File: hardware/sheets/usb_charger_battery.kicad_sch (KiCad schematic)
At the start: 0 parts

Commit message: hw: draw Rev A power tree and USB charger sheets
Power tree: TPS63802 3.3 V logic rail, TPS61023 LED rail with load
disconnect, switched VBAT measurement, VLED sense, 0-ohm measurement
links and test points. The logic rail is enabled by the power switch
or by the charger's power-good output, so USB starts a charging-only
state with the switch off and removing USB turns the rail off again.
The LED rail and VBAT measurement default off.

Charger: USB-C sink with separate 5.1 kOhm Rd, TPD4E05U06 on D+, D-,
CC1 and CC2, isolated CC sensing, BQ25620 switching charger with BC1.2
detection, a board NTC on TS, and the JST-PH battery header.

The VLED setting is provisional until LED testing. The battery header
polarity is provisional until checked against the pack, and the USB-C
receptacle part is still to be chosen.
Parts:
- added C301, C302: 100nF, Capacitor_SMD:C_0402_1005Metric, symbol Device:C
- added C303: 1uF 50V, Capacitor_SMD:C_0603_1608Metric, symbol Device:C
- added C304, C309: 10uF 25V, Capacitor_SMD:C_0805_2012Metric, symbol Device:C
- added C305: 47nF 16V, Capacitor_SMD:C_0402_1005Metric, symbol Device:C
- added C306: 4.7uF 16V, Capacitor_SMD:C_0603_1608Metric, symbol Device:C
- added C307, C308: 22uF 25V, Capacitor_SMD:C_0805_2012Metric, symbol Device:C
- added J301: USB-C receptacle (part TBD), symbol Connector:USB_C_Receptacle_USB2.0_16P
- added J302: Battery JST-PH 2P, Connector_JST:JST_PH_B2B-PH-SM4-TB_1x02-1MP_P2.00mm_Vertical, symbol Connector_Generic_MountingPin:Conn_01x02_MountingPin
- added L301: 1uH, smart-led-badge:L_Coilcraft_XEL4030, symbol Device:L
- added Q301, Q302: AO3400A, Package_TO_SOT_SMD:SOT-23, symbol Transistor_FET:AO3400A
- added R301, R302: 5.1k, Resistor_SMD:R_0402_1005Metric, symbol Device:R
- added R303, R306, R313: 100k, Resistor_SMD:R_0402_1005Metric, symbol Device:R
- added R304, R307: 12k, Resistor_SMD:R_0402_1005Metric, symbol Device:R
- added R309: 5.23k, Resistor_SMD:R_0402_1005Metric, symbol Device:R
- added R310: 30.1k, Resistor_SMD:R_0402_1005Metric, symbol Device:R
- added R311, R312: 10k, Resistor_SMD:R_0402_1005Metric, symbol Device:R
- added R314, R315: 4.7k, Resistor_SMD:R_0402_1005Metric, symbol Device:R
- added TH301: 10k B3380/3434, Resistor_SMD:R_0402_1005Metric, symbol Device:Thermistor_NTC
- added TP301: VBUS, TestPoint:TestPoint_Pad_D1.0mm, symbol Connector:TestPoint
- added TP302: PMID, TestPoint:TestPoint_Pad_D1.0mm, symbol Connector:TestPoint
- added TP303: SYS, TestPoint:TestPoint_Pad_D1.0mm, symbol Connector:TestPoint
- added TP304: VBAT, TestPoint:TestPoint_Pad_D1.0mm, symbol Connector:TestPoint
- added TP305: TS, TestPoint:TestPoint_Pad_D1.0mm, symbol Connector:TestPoint
- added TP306: CHG_PG_N, TestPoint:TestPoint_Pad_D1.0mm, symbol Connector:TestPoint
- added TP307: QON, TestPoint:TestPoint_Pad_D1.0mm, symbol Connector:TestPoint
- added TP308: CHG_STAT, TestPoint:TestPoint_Pad_D1.0mm, symbol Connector:TestPoint
- added TP309: CC1, TestPoint:TestPoint_Pad_D1.0mm, symbol Connector:TestPoint
- added TP310: CC2, TestPoint:TestPoint_Pad_D1.0mm, symbol Connector:TestPoint
- added TP311: GND, TestPoint:TestPoint_Pad_D1.0mm, symbol Connector:TestPoint
- added TP312: I2C1_SDA, TestPoint:TestPoint_Pad_D1.0mm, symbol Connector:TestPoint
- added TP313: I2C1_SCL, TestPoint:TestPoint_Pad_D1.0mm, symbol Connector:TestPoint
- added U301: TPD4E05U06, Package_SON:USON-10_2.5x1.0mm_P0.5mm, symbol Power_Protection:TPD4E05U06DQA
- added U302: BQ25620, smart-led-badge:Texas_RYK0018A, symbol smart-led-badge:BQ25620
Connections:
- new net +3V3: Q301.1 (G), Q302.1 (G), R311.2, R312.2, R314.2, R315.2
- new net BTST: C305.1, U302.1 (BTST)
- new net CC1: J301.A5 (CC1), R301.1, R303.1, TP309.1, U301.4 (D2+)
- new net CC1_HV: Q301.3 (D), R303.2
- new net CC1_SENSE: C301.1, Q301.2 (S), R304.1
- new net CC2: J301.B5 (CC2), R302.1, R306.1, TP310.1, U301.5 (D2-)
- new net CC2_HV: Q302.3 (D), R306.2
- new net CC2_SENSE: C302.1, Q302.2 (S), R307.1
- new net CHG_CE: R313.1, U302.14 (CE)
- new net CHG_INT: R312.1, U302.11 (INT)
- new net CHG_PG_N: TP306.1, U302.3 (PG)
- new net CHG_STAT: R311.1, TP308.1, U302.10 (STAT)
- new net GND: C301.2, C302.2, C303.2, C304.2, C306.2, C307.2, C308.2, C309.2, J301.A1 (GND), J301.A12 (GND), J301.B1 (GND), J301.B12 (GND), J301.SH (SHIELD), J302.1 (Pin_1), J302.MP (MountPin), R301.2, R302.2, R304.2, R307.2, R310.2, R313.2, TH301.2, TP311.1, U301.3 (GND), U301.8 (GND), U302.15 (GND)
- new net I2C1_SCL: R315.1, TP313.1, U302.13 (SCL)
- new net I2C1_SDA: R314.1, TP312.1, U302.12 (SDA)
- new net PMID: C304.1, TP302.1, U302.17 (PMID)
- new net QON: TP307.1, U302.7 (QON)
- new net REGN: C306.1, R309.1, U302.2 (REGN)
- new net SW_CHG: C305.2, L301.1, U302.16 (SW)
- new net SYS: C307.1, C308.1, L301.2, TP303.1, U302.9 (SYS)
- new net TS: R309.2, R310.1, TH301.1, TP305.1, U302.6 (TS)
- new net USB_DN: J301.A7 (D-), J301.B7 (D-), U301.2 (D1-), U302.4 (D-)
- new net USB_DP: J301.A6 (D+), J301.B6 (D+), U301.1 (D1+), U302.5 (D+)
- new net VBAT: C309.1, J302.2 (Pin_2), TP304.1, U302.8 (BAT)
- new net VBUS: C303.1, J301.A4 (VBUS), J301.A9 (VBUS), J301.B4 (VBUS), J301.B9 (VBUS), TP301.1, U302.18 (VBUS)
- no-connect marks 0 -> 6
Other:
- note added: "USB-C, charger and battery (Rev A) - design notes USB-C sink, USB 2.0, no PD: independent 5.1k Rd on CC1/CC2; TPD4E05U06 on D+, D-, CC1, CC2. CC sense: firmware reads CC1/CC2 via SAADC (ratio 0.107) and raises the BQ25620 input limit only on a valid >= 1.5 A advertisement; SDP/unknown sources stay at 100 mA until USB enumeration. BQ25620 (SLUSEG2D): switching charger with NVDC power path, BC1.2 o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"

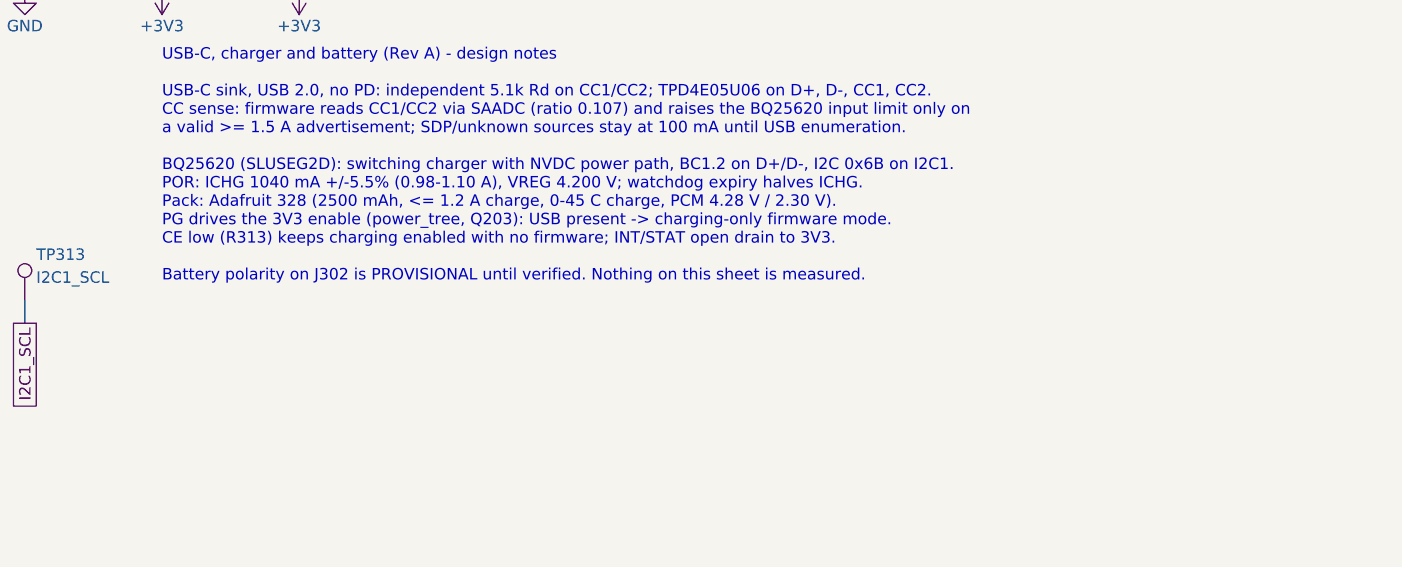
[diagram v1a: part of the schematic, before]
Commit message: hw: set battery header polarity from Adafruit pinout
Keep pin 1 = BAT- and pin 2 = BAT+ on the JST PH header, and record
why: Adafruit's own USB-C Micro-Lipo charger wires its JST PH battery
connector the same way, and Adafruit states the 2500 mAh pack matches
its boards. The "reverse plug" note on the cell drawing describes
that wiring, not a further swap.

No pack is available yet, so bring-up meter-checks each pack before
its first connection.
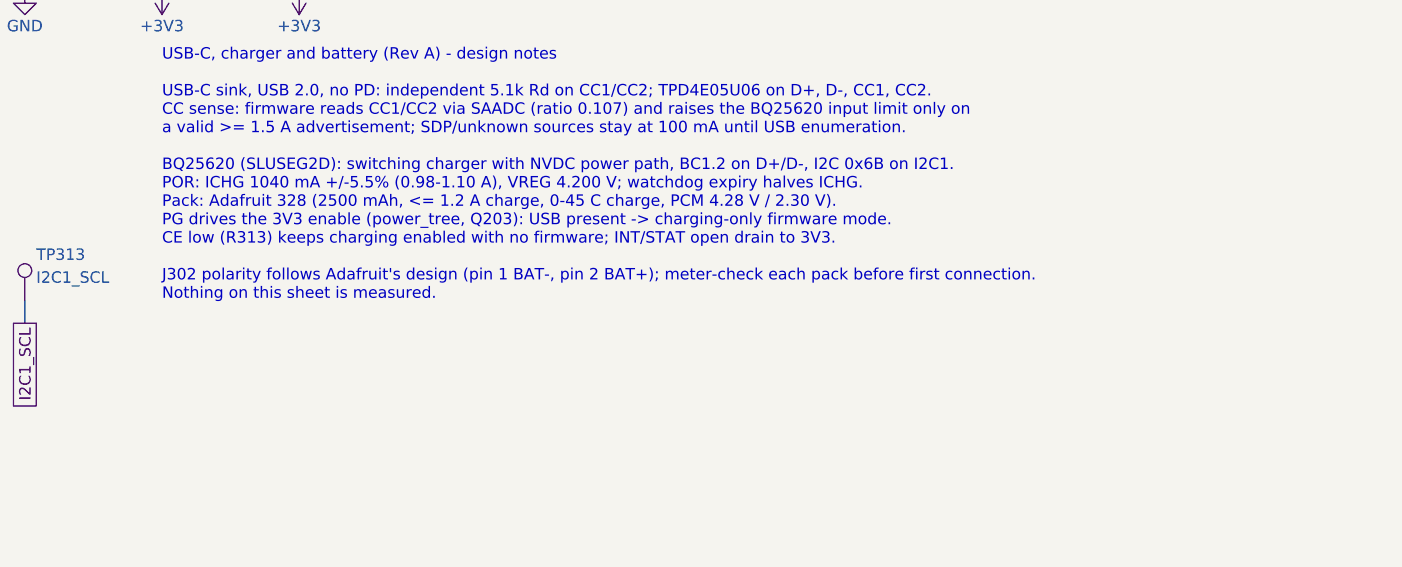
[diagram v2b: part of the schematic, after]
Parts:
- J302: Note POLARITY PROVISIONAL: pin 1 = BAT-, pin 2 = BAT+ until veri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 -> Pin 1 = BAT-, pin 2 = BAT+ per Adafruit's own charger desig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
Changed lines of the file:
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@@
 			)
 		)
-		(property "Note" "POLARITY PROVISIONAL: pin 1 = BAT-, pin 2 = BAT+ until verified against the JST drawing and the Adafruit 328 pack (open decision)"
+		(property "Note" "Pin 1 = BAT-, pin 2 = BAT+ per Adafruit's own charger design (Micro-Lipo USB-C CN2: pin 1 GND, pin 2 VBAT) and Adafruit's statement that product 328 matches its boards; meter-check the pack before first connection"
 			(at 33.02 165.1 0)
 			(hide yes)
@@
 		)
 	)
-	(text "USB-C, charger and battery (Rev A) - design notes\n\nUSB-C sink, USB 2.0, no PD: independent 5.1k Rd on CC1/CC2; TPD4E05U06 on D+, D-, CC1, CC2.\nCC sense: firmware reads CC1/CC2 via SAADC (ratio 0.107) and raises the BQ25620 input limit only on\na valid >= 1.5 A advertisement; SDP/unknown sources stay at 100 mA until USB enumeration.\n\nBQ25620 (SLUSEG2D): switching charger with NVDC power path, BC1.2 on D+/D-, I2C 0x6B on I2C1.\nPOR: ICHG 1040 mA +/-5.5% (0.98-1.10 A), VREG 4.200 V; watchdog expiry halves ICHG.\nPack: Adafruit 328 (2500 mAh, <= 1.2 A charge, 0-45 C charge, PCM 4.28 V / 2.30 V).\nPG drives the 3V3 enable (power_tree, Q203): USB present -> charging-only firmware mode.\nCE low (R313) keeps charging enabled with no firmware; INT/STAT open drain to 3V3.\n\nBattery polarity on J302 is PROVISIONAL until verified. Nothing on this sheet is measured."
+	(text "USB-C, charger and battery (Rev A) - design notes\n\nUSB-C sink, USB 2.0, no PD: independent 5.1k Rd on CC1/CC2; TPD4E05U06 on D+, D-, CC1, CC2.\nCC sense: firmware reads CC1/CC2 via SAADC (ratio 0.107) and raises the BQ25620 input limit only on\na valid >= 1.5 A advertisement; SDP/unknown sources stay at 100 mA until USB enumeration.\n\nBQ25620 (SLUSEG2D): switching charger with NVDC power path, BC1.2 on D+/D-, I2C 0x6B on I2C1.\nPOR: ICHG 1040 mA +/-5.5% (0.98-1.10 A), VREG 4.200 V; watchdog expiry halves ICHG.\nPack: Adafruit 328 (2500 mAh, <= 1.2 A charge, 0-45 C charge, PCM 4.28 V / 2.30 V).\nPG drives the 3V3 enable (power_tree, Q203): USB present -> charging-only firmware mode.\nCE low (R313) keeps charging enabled with no firmware; INT/STAT open drain to 3V3.\n\nJ302 polarity follows Adafruit's design (pin 1 BAT-, pin 2 BAT+); meter-check each pack before first connection.\nNothing on this sheet is measured."
 		(exclude_from_sim no)
 		(at 228.6 177.8 0)
